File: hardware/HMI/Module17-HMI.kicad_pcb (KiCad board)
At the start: 4 copper layers, 96.5 x 80 mm, 59 parts, among them J1 Hirose FH12-26S-0.5SH(55), J3 Hirose FH12A-24S-0.5SH(55), Q1 MMBT3904, Q2 BSS84, SW9 CL-SB-22A-11T, U1 TPS61040DBV, U2 AP7375-33SA, U3 IQS211B00000000TS, U4 CAP1206-x-SL

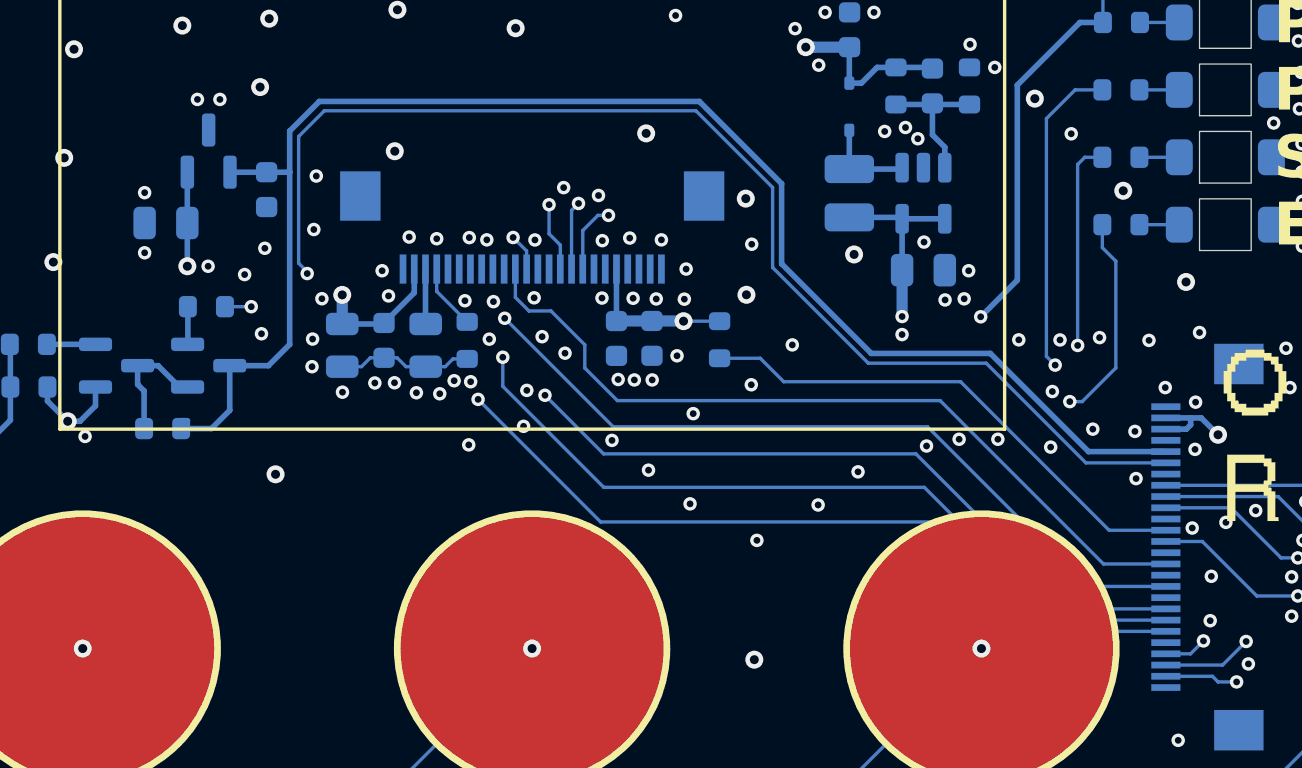
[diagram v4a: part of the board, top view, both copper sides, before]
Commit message: Fixed power button Q2  connected in reverse
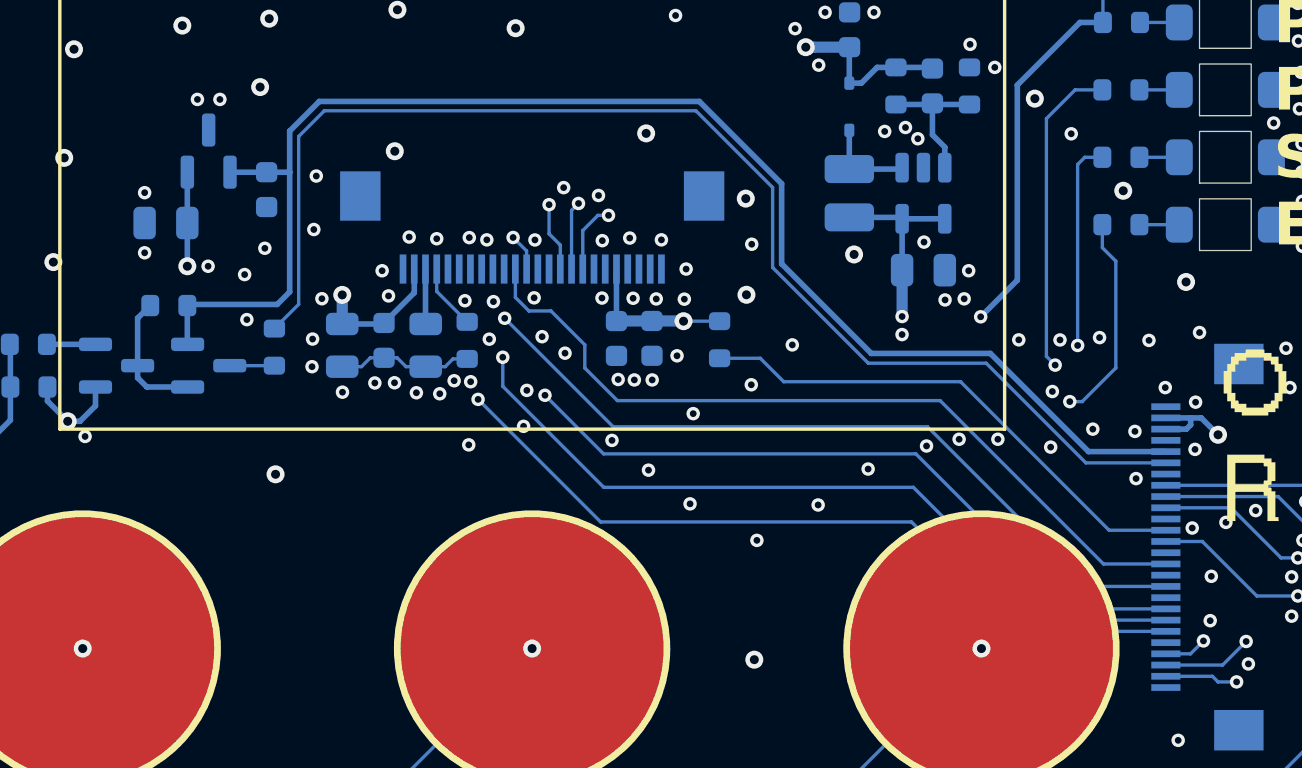
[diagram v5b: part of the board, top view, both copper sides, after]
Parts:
- moved R15 5.48 mm to (195.3, 73.7)
- moved R16 3.52 mm to (200.0, 75.6), turned to 90 degrees
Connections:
- Q2 pad 2: Net-(Q2-S) -> HMI_VIN
- Q2 pad 3: HMI_VIN -> Net-(Q2-D)
- R16 pad 1: Net-(Q2-S) -> Net-(Q2-D)
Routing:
- net HMI_VIN: track 68.1 -> 64.5 mm
- net Net-(Q2-D): track 0.00 -> 1.99 mm
- net Net-(Q2-S): track 1.68 -> 0.00 mm
- net HMI_PWR_ON: track 58.2 -> 56.6 mm, vias 2 -> 0

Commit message: Updated HMI to Rev 0.99b
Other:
- board size 96.5 x 80 mm -> 96.5 x 80.9 mm
- board text added: "96.5000 mm x 80.0000 mm"
- board text added: "Copper Finish:"
- board text added: "HAL SnPb"
- board text added: "Module17 HMI Top panel Rev 0.99b by Morgan ON4MOD"
- board text removed: "91.5000 mm x 80.0000 mm"
- board text removed: "Module17 HMI Top panel Rev 0.99 by Morgan ON4MOD"

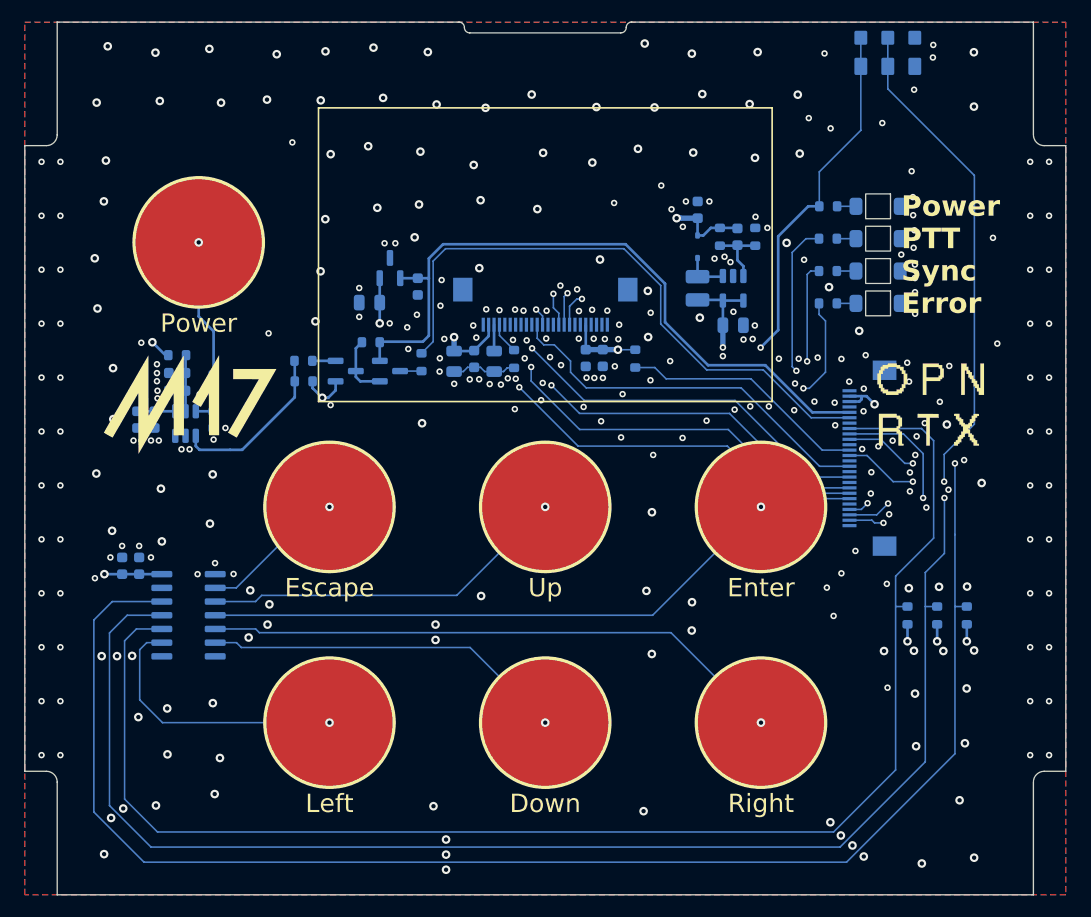
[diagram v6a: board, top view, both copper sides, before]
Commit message: Slightly enlarged HMI PCB
Widened by 0.5mm.
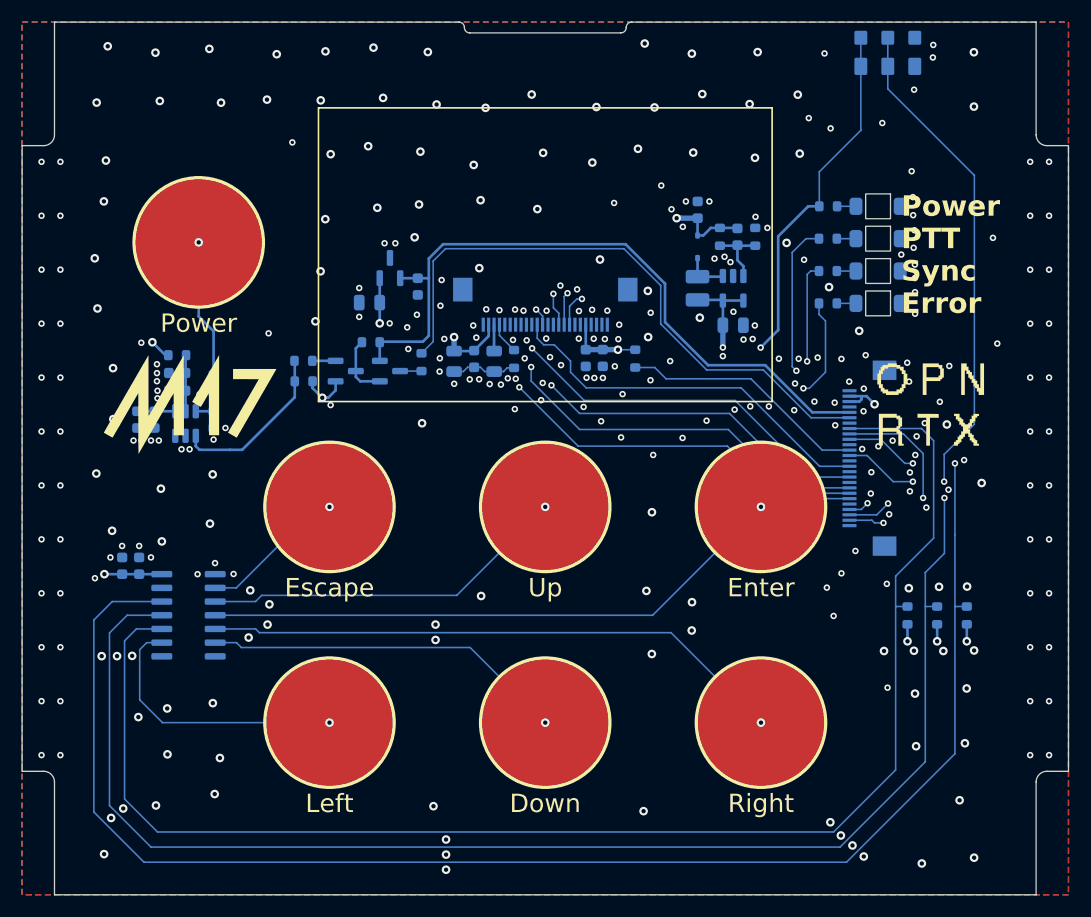
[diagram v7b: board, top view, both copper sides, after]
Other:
- board size 96.5 x 80.9 mm -> 97 x 80.9 mm
- board text added: "97.0000 mm x 80.9000 mm"
- board text removed: "96.5000 mm x 80.0000 mm"

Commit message: Updated HMI PCB to revision 1.0
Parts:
- U4: value CAP1206-x-SL -> CAP1206-1-SL
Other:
- board text added: "Module17 HMI Top panel Rev 1.0 by Morgan ON4MOD"
- board text removed: "Module17 HMI Top panel Rev 0.99b by Morgan ON4MOD"
